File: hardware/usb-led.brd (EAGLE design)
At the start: 15.9 x 15.8 mm, 12 parts, among them U1 Tiny85-20-SMT

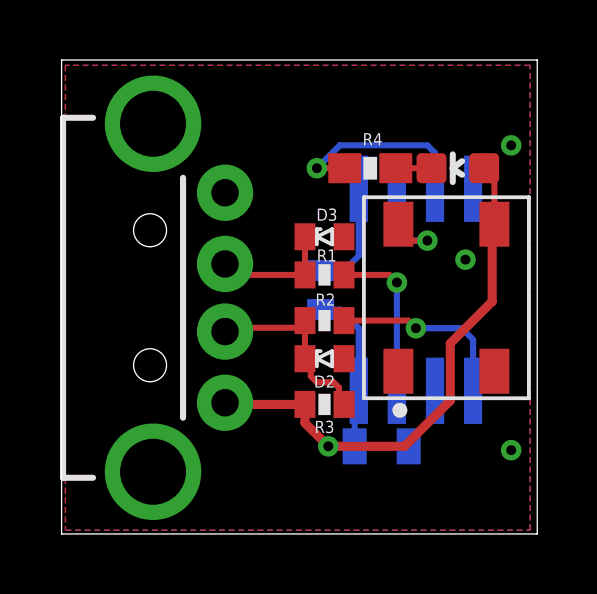
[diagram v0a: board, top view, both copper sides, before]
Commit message: Hardware: revision 2
- Fix: WS2812Bs DIN/DOUT pins were swapped. This was a bug in
  SparkFuns eagle library (fixed in latest version).

- Smaller board: border now cuts through USB plug mounting via.
  OSHPark support said it's fine. We'll see.
  If it doesn't work, I'll have to either use the larger board size,
  find an (expensive) SMD male USB A connector or use a PCB connector
  (and switch to a fab that supports 2.4mm thick boards).

- No 0402 components (R, ZD) anymore. The smallest are 0603 now.
  I can solder 0402, but it's not very beginner-friendly.

- Add 0805 10uF bulk capacitance, just in case. It seems to work fine
  without, so it doesn't need to be populated. (Cost: 18ct at Qty 1)

- Move components that were in the way of my uC test clip.
  I've also added a bKeepout polygon.

- Values for remaining parts (e.g. zener diodes: 3.6V)

- Increase text size from 16mil to 24mil.
  The 16mil texts didn't turn out well.

- Cosmetics.
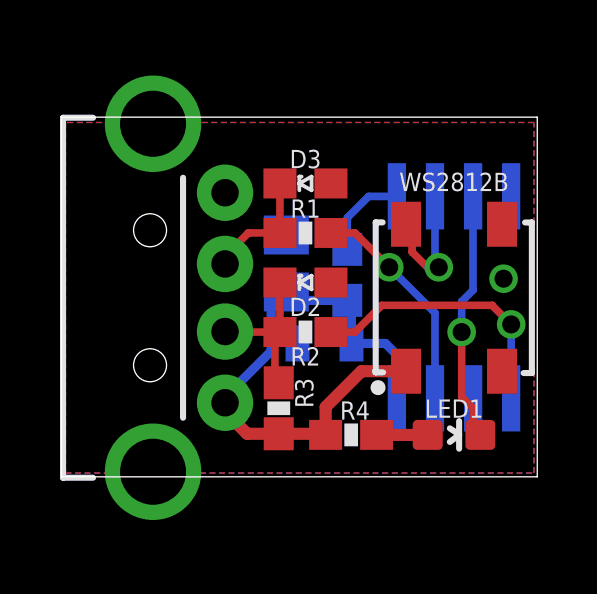
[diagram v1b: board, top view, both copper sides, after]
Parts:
- removed D1: (no value), SparkFun-LED:WS2812B
- added C2: 10uF, rcl:C0805
- added WS2812B: (no value), SparkFun-LED:WS2812B
- D2, D3: value ZD0402 -> 3V6; device z-diode-0402:ZD0402 -> z-diode-0603:ZD0603
- R1, R2, R3, R5: device SparkFun-Passives:0402-RES -> SparkFun-Resistors:0603-RES
- moved R4 8.91 mm to (31.5, 7.11), turned to 180 degrees
- moved LED1 8.89 mm to (34.9, 7.11), turned to 270 degrees
- moved C1 3.92 mm to (30.6, 10.2), turned to 0 degrees
- moved D2 2.62 mm to (30.0, 12.2)
- moved D3 1.89 mm to (30.0, 15.5)
- moved R1 1.53 mm to (30.0, 13.8)
- moved R3 1.53 mm to (29.1, 8.00), turned to 270 degrees
- moved U1 1.30 mm to (34.9, 11.7)
- moved R5 1.02 mm to (31.4, 12.4)
- moved R2 0.74 mm to (30.0, 10.5)
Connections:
- removed net N$7: D1.4, U1.2
- new net DIN: U1.2, WS2812B.4
- net GND: now also C2.2, WS2812B.3; no longer D1.1
- net N$3: now also LED1.C; no longer R4.1
- net N$4: now also LED1.A, R4.1; no longer LED1.C, R4.2
- net VCC: now also C2.1, R4.2, WS2812B.1; no longer D1.3, LED1.A
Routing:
- net DIN: track 0.00 -> 4.60 mm, vias 0 -> 1
- net VCC: track 24.5 -> 20.1 mm, vias 1 -> 0
- net N$7: track 4.10 -> 0.00 mm, vias 1 -> 0
- net D-: track 6.27 -> 9.10 mm
- net N$3: track 6.48 -> 8.42 mm
- net D+: track 5.86 -> 7.42 mm
- net N$2: track 6.53 -> 5.36 mm
- net N$5: track 3.71 -> 3.00 mm
- net N$4: track 1.19 -> 1.81 mm
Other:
- board size 15.9 x 15.8 mm -> 15.9 x 12 mm
- board text added: "USB-LED r2"
- board text removed: "USB-LED r1"

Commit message: Hardware: rename parts
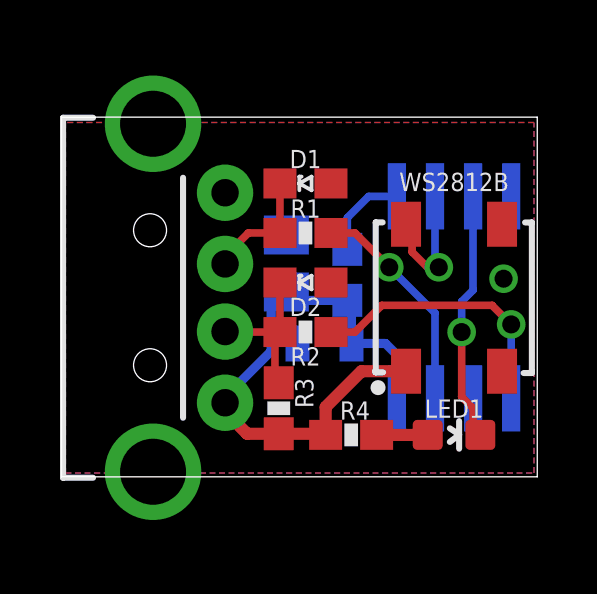
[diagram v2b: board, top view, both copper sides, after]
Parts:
- C1: value (none) -> 10uF; device SparkFun-Passives:0805 -> rcl:C0805
- C2: value 10uF -> (none); device rcl:C0805 -> SparkFun-Passives:0805
- moved C1 2.95 mm to (29.3, 12.8), turned to 90 degrees
- moved C2 2.95 mm to (30.6, 10.2), turned to 0 degrees
- renumbered D3 to D1, JP2 to USB, U1 to IC1
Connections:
- net N$1 renamed EXT_D+
- net N$2 renamed EXT_D-
- net N$5 renamed C10
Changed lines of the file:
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@@
 </autorouter>
 <elements>
-<element name="U1" library="SparkFun-DigitalIC" package="SO08-EIAJ" value="Tiny85-20-SMT" x="34.925" y="11.684" smashed="yes" rot="MR180">
+<element name="IC1" library="SparkFun-DigitalIC" package="SO08-EIAJ" value="Tiny85-20-SMT" x="34.925" y="11.684" smashed="yes" rot="MR180">
 <attribute name="PROD_ID" value="IC-09092" x="34.925" y="11.684" size="1.778" layer="28" rot="MR180" display="off"/>
+<attribute name="VALUE" x="33.655" y="13.081" size="0.4064" layer="28" rot="MR180"/>
+<attribute name="NAME" x="34.163" y="11.938" size="0.6096" layer="26" font="vector" rot="MR180"/>
 </element>
 <element name="R1" library="SparkFun-Resistors" package="0603-RES" value="68R" x="29.972" y="13.843" smashed="yes" rot="R180">
@@
 <attribute name="VALUE" x="28.067" y="8.5725" size="0.4064" layer="27" rot="R270"/>
 </element>
-<element name="C1" library="SparkFun-Passives" package="0805" value="" x="30.607" y="10.16" smashed="yes" rot="MR0">
+<element name="C2" library="SparkFun-Passives" package="0805" value="" x="30.607" y="10.16" smashed="yes" rot="MR0">
 <attribute name="NAME" x="30.607" y="9.2075" size="0.6096" layer="26" font="vector" rot="MR0" align="top-center"/>
 <attribute name="VALUE" x="31.623" y="8.763" size="0.4064" layer="28" rot="MR0"/>
@@
 </element>
 <element name="R5" library="SparkFun-Resistors" package="0603-RES" value="10K" x="31.369" y="12.446" smashed="yes" rot="MR90">
-<attribute name="NAME" x="31.369" y="14.097" size="0.6096" layer="26" font="vector" rot="MR90" align="center-left"/>
+<attribute name="NAME" x="31.369" y="14.732" size="0.6096" layer="26" font="vector" rot="MR90" align="center-left"/>
 <attribute name="VALUE" x="30.226" y="11.3665" size="0.4064" layer="28" rot="MR90"/>
 </element>
-<element name="JP2" library="SparkFun-Connectors" package="USB-A-H" value="USB-A-H" x="24.892" y="11.684" smashed="yes"/>
+<element name="USB" library="SparkFun-Connectors" package="USB-A-H" value="USB-A-H" x="24.892" y="11.684" smashed="yes"/>
 <element name="WS2812B" library="SparkFun-LED" package="WS2812B" value="" x="34.925" y="11.684" smashed="yes" rot="R90">
 <attribute name="NAME" x="34.925" y="15.24" size="0.6096" layer="25" font="vector" rot="R180" align="top-center"/>
@@
 <attribute name="VALUE" x="30.988" y="13.335" size="0.4064" layer="27" font="vector" rot="R180"/>
 </element>
-<element name="D3" library="z-diode-0603" package="ZD0603" value="3V6" x="29.972" y="15.494" smashed="yes" rot="R180">
+<element name="D1" library="z-diode-0603" package="ZD0603" value="3V6" x="29.972" y="15.494" smashed="yes" rot="R180">
 <attribute name="NAME" x="29.972" y="16.002" size="0.6096" layer="25" font="vector" rot="R180" align="top-center"/>
 <attribute name="VALUE" x="30.988" y="16.637" size="0.4064" layer="27" font="vector" rot="R180"/>
 </element>
-<element name="C2" library="rcl" package="C0805" value="10uF" x="29.337" y="12.827" smashed="yes" rot="MR90">
+<element name="C1" library="rcl" package="C0805" value="10uF" x="29.337" y="12.827" smashed="yes" rot="MR90">
 <attribute name="NAME" x="29.337" y="14.732" size="0.6096" layer="26" font="vector" rot="MR90" align="center-left"/>
 <attribute name="VALUE" x="26.797" y="11.557" size="1.27" layer="28" rot="MR90"/>
@@
 <signals>
 <signal name="GND">
-<contactref element="U1" pad="4"/>
+<contactref element="IC1" pad="4"/>
 <polygon width="0.3048" layer="16">
 <vertex x="21.971" y="5.842"/>
@@
 <vertex x="21.971" y="17.526"/>
 </polygon>
-<contactref element="C1" pad="2"/>
-<contactref element="JP2" pad="GND"/>
+<contactref element="C2" pad="2"/>
+<contactref element="USB" pad="GND"/>
 <contactref element="WS2812B" pad="3"/>
 <contactref element="D2" pad="A"/>
-<contactref element="D3" pad="A"/>
-<contactref element="C2" pad="2"/>
+<contactref element="D1" pad="A"/>
+<contactref element="C1" pad="2"/>
 <via x="36.576" y="12.319" extent="1-16" drill="0.6"/>
 </signal>
 <signal name="VCC">
-<contactref element="U1" pad="8"/>
+<contactref element="IC1" pad="8"/>
 <contactref element="R3" pad="2"/>
-<contactref element="C1" pad="1"/>
+<contactref element="C2" pad="1"/>
 <contactref element="R5" pad="1"/>
-<contactref element="JP2" pad="VBUS"/>
+<contactref element="USB" pad="VBUS"/>
 <contactref element="WS2812B" pad="1"/>
 <wire x1="33.401" y1="9.158" x2="33.325" y2="9.234" width="0.4064" layer="1"/>
 <wire x1="33.02" y1="8.3312" x2="32.9548" y2="8.266" width="0.254" layer="16"/>
-<contactref element="C2" pad="1"/>
+<contactref element="C1" pad="1"/>
 <contactref element="R4" pad="2"/>
 <wire x1="30.646" y1="7.112" x2="30.48" y2="7.151" width="0.254" layer="1"/>
@@
 <wire x1="33.02" y1="9.779" x2="33.02" y2="8.3312" width="0.3048" layer="16"/>
 </signal>
-<signal name="N$2">
+<signal name="EXT_D-">
 <contactref element="R2" pad="2"/>
 <contactref element="R3" pad="1"/>
-<contactref element="JP2" pad="D-"/>
+<contactref element="USB" pad="D-"/>
 <contactref element="D2" pad="K"/>
 <wire x1="29.122" y1="10.541" x2="27.308" y2="10.541" width="0.254" layer="1"/>
@@
 <signal name="D-">
 <contactref element="R2" pad="1"/>
-<contactref element="U1" pad="5"/>
+<contactref element="IC1" pad="5"/>
 <via x="36.83" y="10.795" extent="1-16" drill="0.6"/>
 <wire x1="36.83" y1="10.795" x2="36.83" y2="8.3312" width="0.254" layer="16"/>
@@
 <signal name="D+">
 <contactref element="R1" pad="1"/>
-<contactref element="U1" pad="7"/>
+<contactref element="IC1" pad="7"/>
 <via x="32.766" y="12.7" extent="1-16" drill="0.6"/>
 <wire x1="32.766" y1="12.7" x2="31.623" y2="13.843" width="0.254" layer="1"/>
@@
 <wire x1="31.623" y1="13.843" x2="30.822" y2="13.843" width="0.254" layer="1"/>
 </signal>
-<signal name="N$5">
+<signal name="C10">
 <contactref element="R5" pad="2"/>
-<contactref element="U1" pad="1"/>
+<contactref element="IC1" pad="1"/>
 <wire x1="33.02" y1="15.0622" x2="32.0802" y2="15.0622" width="0.254" layer="16"/>
 <wire x1="32.0802" y1="15.0622" x2="31.369" y2="14.351" width="0.254" layer="16"/>
 <wire x1="31.369" y1="14.351" x2="31.369" y2="13.296" width="0.254" layer="16"/>
 </signal>
-<signal name="N$1">
-<contactref element="JP2" pad="D+"/>
+<signal name="EXT_D+">
+<contactref element="USB" pad="D+"/>
 <contactref element="R1" pad="2"/>
-<contactref element="D3" pad="K"/>
+<contactref element="D1" pad="K"/>
 <wire x1="29.122" y1="13.843" x2="29.122" y2="15.494" width="0.254" layer="1"/>
 <wire x1="29.122" y1="13.843" x2="28.067" y2="13.843" width="0.254" layer="1"/>
@@
 </signal>
 <signal name="DIN">
-<contactref element="U1" pad="2"/>
+<contactref element="IC1" pad="2"/>
 <contactref element="WS2812B" pad="4"/>
 <via x="34.417" y="12.7" extent="1-16" drill="0.6"/>
@@
 <signal name="N$3">
 <contactref element="LED1" pad="C"/>
-<contactref element="U1" pad="3"/>
+<contactref element="IC1" pad="3"/>
 <wire x1="35.802" y1="7.112" x2="35.56" y2="7.227" width="0.254" layer="1"/>
 <via x="35.179" y="10.541" extent="1-16" drill="0.6"/>

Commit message: Hardware: more space for the Zener diodes
Their case is a a little bit larger than the normal 0603 footprint.
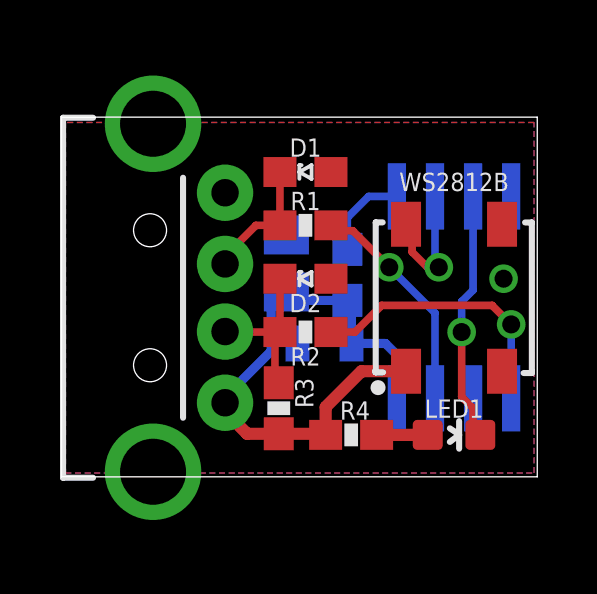
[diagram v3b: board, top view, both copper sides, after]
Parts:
- C2: value (none) -> 100nF
- moved D1 0.38 mm to (30.0, 15.9)
- moved R1 0.25 mm to (30.0, 14.1)
- moved D2 0.13 mm to (30.0, 12.3)
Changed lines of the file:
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@@
 <attribute name="NAME" x="34.163" y="11.938" size="0.6096" layer="26" font="vector" rot="MR180"/>
 </element>
-<element name="R1" library="SparkFun-Resistors" package="0603-RES" value="68R" x="29.972" y="13.843" smashed="yes" rot="R180">
-<attribute name="NAME" x="29.972" y="14.351" size="0.6096" layer="25" font="vector" rot="R180" align="top-center"/>
-<attribute name="VALUE" x="30.5435" y="13.335" size="0.4064" layer="27" rot="R180"/>
+<element name="R1" library="SparkFun-Resistors" package="0603-RES" value="68R" x="29.972" y="14.097" smashed="yes" rot="R180">
+<attribute name="NAME" x="29.972" y="14.605" size="0.6096" layer="25" font="vector" rot="R180" align="top-center"/>
+<attribute name="VALUE" x="30.5435" y="13.589" size="0.4064" layer="27" rot="R180"/>
 </element>
 <element name="R2" library="SparkFun-Resistors" package="0603-RES" value="68R" x="29.972" y="10.541" smashed="yes" rot="R180">
@@
 <attribute name="VALUE" x="28.067" y="8.5725" size="0.4064" layer="27" rot="R270"/>
 </element>
-<element name="C2" library="SparkFun-Passives" package="0805" value="" x="30.607" y="10.16" smashed="yes" rot="MR0">
+<element name="C2" library="SparkFun-Passives" package="0805" value="100nF" x="30.607" y="10.16" smashed="yes" rot="MR0">
 <attribute name="NAME" x="30.607" y="9.2075" size="0.6096" layer="26" font="vector" rot="MR0" align="top-center"/>
 <attribute name="VALUE" x="31.623" y="8.763" size="0.4064" layer="28" rot="MR0"/>
@@
 <attribute name="VALUE" x="36.525" y="15.684" size="0.6096" layer="27" rot="R90"/>
 </element>
-<element name="D2" library="z-diode-0603" package="ZD0603" value="3V6" x="29.972" y="12.192" smashed="yes" rot="R180">
-<attribute name="NAME" x="29.972" y="11.684" size="0.6096" layer="25" font="vector" rot="R180" align="bottom-center"/>
-<attribute name="VALUE" x="30.988" y="13.335" size="0.4064" layer="27" font="vector" rot="R180"/>
+<element name="D2" library="z-diode-0603" package="ZD0603" value="3V6" x="29.972" y="12.319" smashed="yes" rot="R180">
+<attribute name="NAME" x="29.972" y="11.811" size="0.6096" layer="25" font="vector" rot="R180" align="bottom-center"/>
+<attribute name="VALUE" x="30.988" y="13.462" size="0.4064" layer="27" font="vector" rot="R180"/>
 </element>
-<element name="D1" library="z-diode-0603" package="ZD0603" value="3V6" x="29.972" y="15.494" smashed="yes" rot="R180">
-<attribute name="NAME" x="29.972" y="16.002" size="0.6096" layer="25" font="vector" rot="R180" align="top-center"/>
-<attribute name="VALUE" x="30.988" y="16.637" size="0.4064" layer="27" font="vector" rot="R180"/>
+<element name="D1" library="z-diode-0603" package="ZD0603" value="3V6" x="29.972" y="15.875" smashed="yes" rot="R180">
+<attribute name="NAME" x="29.972" y="16.383" size="0.6096" layer="25" font="vector" rot="R180" align="top-center"/>
+<attribute name="VALUE" x="30.988" y="17.018" size="0.4064" layer="27" font="vector" rot="R180"/>
 </element>
 <element name="C1" library="rcl" package="C0805" value="10uF" x="29.337" y="12.827" smashed="yes" rot="MR90">
@@
 <wire x1="29.122" y1="10.541" x2="27.308" y2="10.541" width="0.254" layer="1"/>
 <wire x1="27.308" y1="10.541" x2="27.292" y2="10.557" width="0.254" layer="1"/>
-<wire x1="29.122" y1="10.541" x2="29.122" y2="12.192" width="0.254" layer="1"/>
 <wire x1="28.956" y1="10.502" x2="29.122" y2="10.541" width="0.254" layer="1"/>
 <wire x1="28.956" y1="10.502" x2="28.956" y2="8.978" width="0.254" layer="1"/>
 <wire x1="28.956" y1="8.978" x2="29.083" y2="8.851" width="0.254" layer="1"/>
+<wire x1="29.122" y1="10.541" x2="29.122" y2="12.319" width="0.254" layer="1"/>
 </signal>
 <signal name="D-">
@@
 <wire x1="32.512" y1="11.43" x2="36.195" y2="11.43" width="0.254" layer="1"/>
 <wire x1="36.195" y1="11.43" x2="36.83" y2="10.795" width="0.254" layer="1"/>
-<wire x1="30.822" y1="10.541" x2="31.623" y2="10.541" width="0.254" layer="1"/>
 <wire x1="31.623" y1="10.541" x2="32.512" y2="11.43" width="0.254" layer="1"/>
+<wire x1="31.623" y1="10.541" x2="30.822" y2="10.541" width="0.254" layer="1"/>
 </signal>
 <signal name="D+">
@@
 <contactref element="IC1" pad="7"/>
 <via x="32.766" y="12.7" extent="1-16" drill="0.6"/>
-<wire x1="32.766" y1="12.7" x2="31.623" y2="13.843" width="0.254" layer="1"/>
 <wire x1="32.766" y1="12.7" x2="34.29" y2="11.176" width="0.254" layer="16"/>
 <wire x1="34.29" y1="11.176" x2="34.29" y2="8.3312" width="0.254" layer="16"/>
-<wire x1="31.623" y1="13.843" x2="30.822" y2="13.843" width="0.254" layer="1"/>
+<wire x1="32.766" y1="12.7" x2="31.5468" y2="13.9192" width="0.254" layer="1"/>
+<wire x1="31.5468" y1="13.9192" x2="30.9998" y2="13.9192" width="0.254" layer="1"/>
+<wire x1="30.9998" y1="13.9192" x2="30.822" y2="14.097" width="0.254" layer="1"/>
 </signal>
 <signal name="C10">
@@
 <contactref element="R1" pad="2"/>
 <contactref element="D1" pad="K"/>
-<wire x1="29.122" y1="13.843" x2="29.122" y2="15.494" width="0.254" layer="1"/>
-<wire x1="29.122" y1="13.843" x2="28.067" y2="13.843" width="0.254" layer="1"/>
-<wire x1="28.067" y1="13.843" x2="27.292" y2="13.068" width="0.254" layer="1"/>
+<wire x1="29.122" y1="14.097" x2="29.122" y2="15.875" width="0.254" layer="1"/>
+<wire x1="28.321" y1="14.097" x2="27.292" y2="13.068" width="0.254" layer="1"/>
 <wire x1="27.292" y1="13.068" x2="27.292" y2="12.811" width="0.254" layer="1"/>
+<wire x1="28.321" y1="14.097" x2="29.122" y2="14.097" width="0.254" layer="1"/>
 </signal>
 <signal name="DIN">
